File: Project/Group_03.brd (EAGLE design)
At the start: 100 x 80 mm, 29 parts, among them J1 POWER_JACKPTH_LOCK, U1 +12v, U3 TCA9546APW, U4 TMUX1208RSV

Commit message: Moved CY8CKIT
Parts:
- moved U$1 3.81 mm to (55.9, 34.3)
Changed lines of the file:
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@@
 <attribute name="VALUE" x="19.177" y="73.66" size="0.6096" layer="27" font="vector" ratio="20" rot="R270" align="top-center"/>
 </element>
-<element name="U$1" library="CY8KIT-059" package="CY8CKIT-059_TARGET" value="CY8CKIT-059_TARGET" x="55.88" y="38.1" smashed="yes" rot="R270"/>
+<element name="U$1" library="CY8KIT-059" package="CY8CKIT-059_TARGET" value="CY8CKIT-059_TARGET" x="55.88" y="34.29" smashed="yes" rot="R270"/>
 <element name="U1" library="SparkFun-IC-Power" package="TO-252" value="+12v" x="7.62" y="60.96" smashed="yes" rot="R90">
 <attribute name="NAME" x="10.16" y="57.15" size="1.27" layer="25" rot="R180"/>
@@
 <wire x1="76.87" y1="63.43" x2="82.423" y2="71.12" width="0" layer="19" extent="1-1"/>
 <wire x1="78.27" y1="62.43" x2="76.87" y2="63.43" width="0" layer="19" extent="1-1"/>
-<wire x1="64.77" y1="71.12" x2="76.87" y2="63.43" width="0" layer="19" extent="1-1"/>
+<wire x1="64.77" y1="67.31" x2="76.87" y2="63.43" width="0" layer="19" extent="1-1"/>
 <wire x1="77.735" y1="32.11" x2="78.27" y2="62.43" width="0" layer="19" extent="1-1"/>
-<wire x1="25.273" y1="62.23" x2="64.77" y2="71.12" width="0" layer="19" extent="1-1"/>
+<wire x1="25.273" y1="62.23" x2="64.77" y2="67.31" width="0" layer="19" extent="1-1"/>
 <wire x1="12.42" y1="63.24" x2="25.273" y2="62.23" width="0" layer="19" extent="1-1"/>
 <wire x1="3.81" y1="40.64" x2="12.42" y2="63.24" width="0" layer="19" extent="1-1"/>
 <wire x1="22.86" y1="37.37" x2="3.81" y2="40.64" width="0" layer="19" extent="1-1"/>
 <wire x1="22.86" y1="31.75" x2="22.86" y2="37.37" width="0" layer="19" extent="1-1"/>
-<wire x1="44.45" y1="7.62" x2="22.86" y2="31.75" width="0" layer="19" extent="1-1"/>
+<wire x1="44.45" y1="3.81" x2="22.86" y2="31.75" width="0" layer="19" extent="1-1"/>
 </signal>
 <signal name="GND">
@@
 <contactref element="U4" pad="12"/>
 <wire x1="78.27" y1="62.83" x2="85.217" y2="71.12" width="0" layer="19" extent="1-1"/>
-<wire x1="64.77" y1="68.58" x2="78.27" y2="62.83" width="0" layer="19" extent="1-1"/>
+<wire x1="64.77" y1="64.77" x2="78.27" y2="62.83" width="0" layer="19" extent="1-1"/>
 <wire x1="79.035" y1="26.31" x2="78.27" y2="62.83" width="0" layer="19" extent="1-1"/>
 <wire x1="82.285" y1="26.31" x2="79.035" y2="26.31" width="0" layer="19" extent="1-1"/>
-<wire x1="28.067" y1="62.23" x2="64.77" y2="68.58" width="0" layer="19" extent="1-1"/>
+<wire x1="28.067" y1="62.23" x2="64.77" y2="64.77" width="0" layer="19" extent="1-1"/>
 <wire x1="21.22" y1="64.77" x2="28.067" y2="62.23" width="0" layer="19" extent="1-1"/>
 <wire x1="25.4" y1="52.07" x2="28.067" y2="62.23" width="0" layer="19" extent="1-1"/>
@@
 <wire x1="22.86" y1="29.21" x2="22.86" y2="47.84" width="0" layer="19" extent="1-1"/>
 <wire x1="3.81" y1="38.1" x2="22.86" y2="29.21" width="0" layer="19" extent="1-1"/>
-<wire x1="44.45" y1="10.16" x2="22.86" y2="29.21" width="0" layer="19" extent="1-1"/>
+<wire x1="44.45" y1="6.35" x2="22.86" y2="29.21" width="0" layer="19" extent="1-1"/>
 </signal>
 <signal name="PHOTO_OUT">
@@
 <contactref element="R11" pad="2"/>
 <contactref element="U$1" pad="44"/>
-<wire x1="22.86" y1="46.14" x2="44.45" y2="50.8" width="0" layer="19" extent="1-1"/>
+<wire x1="22.86" y1="46.14" x2="44.45" y2="46.99" width="0" layer="19" extent="1-1"/>
 <wire x1="22.86" y1="41.37" x2="22.86" y2="46.14" width="0" layer="19" extent="1-1"/>
 </signal>
@@
 <contactref element="U2" pad="2"/>
 <contactref element="U$1" pad="43"/>
-<wire x1="24.765" y1="30.48" x2="44.45" y2="48.26" width="0" layer="19" extent="1-1"/>
+<wire x1="24.765" y1="30.48" x2="44.45" y2="44.45" width="0" layer="19" extent="1-1"/>
 </signal>
 <signal name="I2C_SCL_0">
@@
 <contactref element="U3" pad="1"/>
 <contactref element="U$1" pad="6"/>
-<wire x1="64.77" y1="20.32" x2="77.735" y2="26.31" width="0" layer="19" extent="1-1"/>
+<wire x1="64.77" y1="16.51" x2="77.735" y2="26.31" width="0" layer="19" extent="1-1"/>
 </signal>
 <signal name="I2C_A1">
 <contactref element="U3" pad="2"/>
 <contactref element="U$1" pad="7"/>
-<wire x1="64.77" y1="22.86" x2="78.385" y2="26.31" width="0" layer="19" extent="1-1"/>
+<wire x1="64.77" y1="19.05" x2="78.385" y2="26.31" width="0" layer="19" extent="1-1"/>
 </signal>
 <signal name="I2C_A2">
 <contactref element="U3" pad="13"/>
 <contactref element="U$1" pad="8"/>
-<wire x1="64.77" y1="25.4" x2="79.685" y2="32.11" width="0" layer="19" extent="1-1"/>
+<wire x1="64.77" y1="21.59" x2="79.685" y2="32.11" width="0" layer="19" extent="1-1"/>
 </signal>
 <signal name="I2C_SDA">
 <contactref element="U3" pad="15"/>
 <contactref element="U$1" pad="15"/>
-<wire x1="64.77" y1="43.18" x2="78.385" y2="32.11" width="0" layer="19" extent="1-1"/>
+<wire x1="64.77" y1="39.37" x2="78.385" y2="32.11" width="0" layer="19" extent="1-1"/>
 </signal>
 <signal name="I2C_SCL">
 <contactref element="U3" pad="14"/>
 <contactref element="U$1" pad="16"/>
-<wire x1="64.77" y1="45.72" x2="79.035" y2="32.11" width="0" layer="19" extent="1-1"/>
+<wire x1="64.77" y1="41.91" x2="79.035" y2="32.11" width="0" layer="19" extent="1-1"/>
 </signal>
 <signal name="N$3">
 <contactref element="U$1" pad="32"/>
 <contactref element="J6" pad="1"/>
-<wire x1="2.54" y1="6.35" x2="44.45" y2="20.32" width="0" layer="19" extent="1-1"/>
+<wire x1="2.54" y1="6.35" x2="44.45" y2="16.51" width="0" layer="19" extent="1-1"/>
 </signal>
 <signal name="N$4">
 <contactref element="U$1" pad="33"/>
 <contactref element="J6" pad="2"/>
-<wire x1="2.794" y1="8.89" x2="44.45" y2="22.86" width="0" layer="19" extent="1-1"/>
+<wire x1="2.794" y1="8.89" x2="44.45" y2="19.05" width="0" layer="19" extent="1-1"/>
 </signal>
 <signal name="N$5">
 <contactref element="U$1" pad="34"/>
 <contactref element="J6" pad="3"/>
-<wire x1="2.54" y1="11.43" x2="44.45" y2="25.4" width="0" layer="19" extent="1-1"/>
+<wire x1="2.54" y1="11.43" x2="44.45" y2="21.59" width="0" layer="19" extent="1-1"/>
 </signal>
 <signal name="N$6">
 <contactref element="U$1" pad="35"/>
 <contactref element="J6" pad="4"/>
-<wire x1="2.794" y1="13.97" x2="44.45" y2="27.94" width="0" layer="19" extent="1-1"/>
+<wire x1="2.794" y1="13.97" x2="44.45" y2="24.13" width="0" layer="19" extent="1-1"/>
 </signal>
 <signal name="N$7">
 <contactref element="U$1" pad="36"/>
 <contactref element="J6" pad="5"/>
-<wire x1="2.54" y1="16.51" x2="44.45" y2="30.48" width="0" layer="19" extent="1-1"/>
+<wire x1="2.54" y1="16.51" x2="44.45" y2="26.67" width="0" layer="19" extent="1-1"/>
 </signal>
 <signal name="N$8">
 <contactref element="U$1" pad="37"/>
 <contactref element="J6" pad="6"/>
-<wire x1="2.794" y1="19.05" x2="44.45" y2="33.02" width="0" layer="19" extent="1-1"/>
+<wire x1="2.794" y1="19.05" x2="44.45" y2="29.21" width="0" layer="19" extent="1-1"/>
 </signal>
 <signal name="N$9">
 <contactref element="U$1" pad="51"/>
 <contactref element="D1" pad="A"/>
-<wire x1="39.6" y1="55.88" x2="44.45" y2="68.58" width="0" layer="19" extent="1-1"/>
+<wire x1="39.6" y1="55.88" x2="44.45" y2="64.77" width="0" layer="19" extent="1-1"/>
 </signal>
 <signal name="N$11">
@@
 <contactref element="U$1" pad="21"/>
 <contactref element="U4" pad="6"/>
-<wire x1="64.77" y1="58.42" x2="77.27" y2="61.03" width="0" layer="19" extent="1-1"/>
+<wire x1="64.77" y1="54.61" x2="77.27" y2="61.03" width="0" layer="19" extent="1-1"/>
 </signal>
 <signal name="MUX_A2">
 <contactref element="U$1" pad="22"/>
 <contactref element="U4" pad="13"/>
-<wire x1="64.77" y1="60.96" x2="78.07" y2="63.43" width="0" layer="19" extent="1-1"/>
+<wire x1="64.77" y1="57.15" x2="78.07" y2="63.43" width="0" layer="19" extent="1-1"/>
 </signal>
 <signal name="MUX_A1">
 <contactref element="U$1" pad="23"/>
 <contactref element="U4" pad="14"/>
-<wire x1="64.77" y1="63.5" x2="77.67" y2="63.43" width="0" layer="19" extent="1-1"/>
+<wire x1="64.77" y1="59.69" x2="77.67" y2="63.43" width="0" layer="19" extent="1-1"/>
 </signal>
 <signal name="MUX_A0">
 <contactref element="U$1" pad="24"/>
 <contactref element="U4" pad="15"/>
-<wire x1="64.77" y1="66.04" x2="77.27" y2="63.43" width="0" layer="19" extent="1-1"/>
+<wire x1="64.77" y1="62.23" x2="77.27" y2="63.43" width="0" layer="19" extent="1-1"/>
 </signal>
 <signal name="N$2">

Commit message: First board layout attempt
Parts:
- moved J6 99.6 mm to (97.8, 35.6)
- moved J7 35.2 mm to (19.1, 6.35)
- moved R5 24.4 mm to (92.7, 17.8), turned to 270 degrees
- moved R4 23.4 mm to (92.7, 21.6), turned to 90 degrees
- moved R3 21.6 mm to (92.7, 2.54), turned to 90 degrees
- moved R11 19.0 mm to (41.9, 47.0)
- moved U2 16.6 mm to (39.4, 31.8)
- moved R2 16.5 mm to (92.7, 6.35), turned to 90 degrees
- moved U4 15.2 mm to (92.7, 62.2)
- moved R7 14.5 mm to (92.7, 25.4), turned to 90 degrees
- moved R10 14.0 mm to (36.8, 39.4)
- moved U3 13.7 mm to (85.1, 16.5)
- moved R1 13.3 mm to (41.9, 55.9), turned to 90 degrees
- moved J4 12.7 mm to (97.8, 22.9), turned to 90 degrees
- moved J2 12.7 mm to (97.8, 10.2), turned to 90 degrees
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
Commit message: Parts placement (size 73.66x71.12)
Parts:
- moved J7 37.0 mm to (55.9, 10.2), turned to 270 degrees
- moved D1 36.8 mm to (15.2, 39.4)
- moved R1 36.8 mm to (15.2, 30.5)
- moved R11 36.8 mm to (15.2, 21.6)
- moved R10 34.3 mm to (10.2, 17.8)
- moved S1 27.5 mm to (5.08, 58.4)
- moved R2 27.1 mm to (66.0, 11.4)
- moved R3 27.1 mm to (66.0, 7.62)
- moved R4 27.1 mm to (66.0, 26.7)
- moved R5 27.1 mm to (66.0, 22.9)
- moved R6 27.1 mm to (66.0, 34.3)
- moved R7 27.1 mm to (66.0, 30.5)
- moved R8 27.1 mm to (66.0, 19.1)
- moved R9 27.1 mm to (66.0, 15.2)
- moved J2 26.8 mm to (71.1, 7.62)
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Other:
- board size 100 x 80 mm -> 73.7 x 71.1 mm

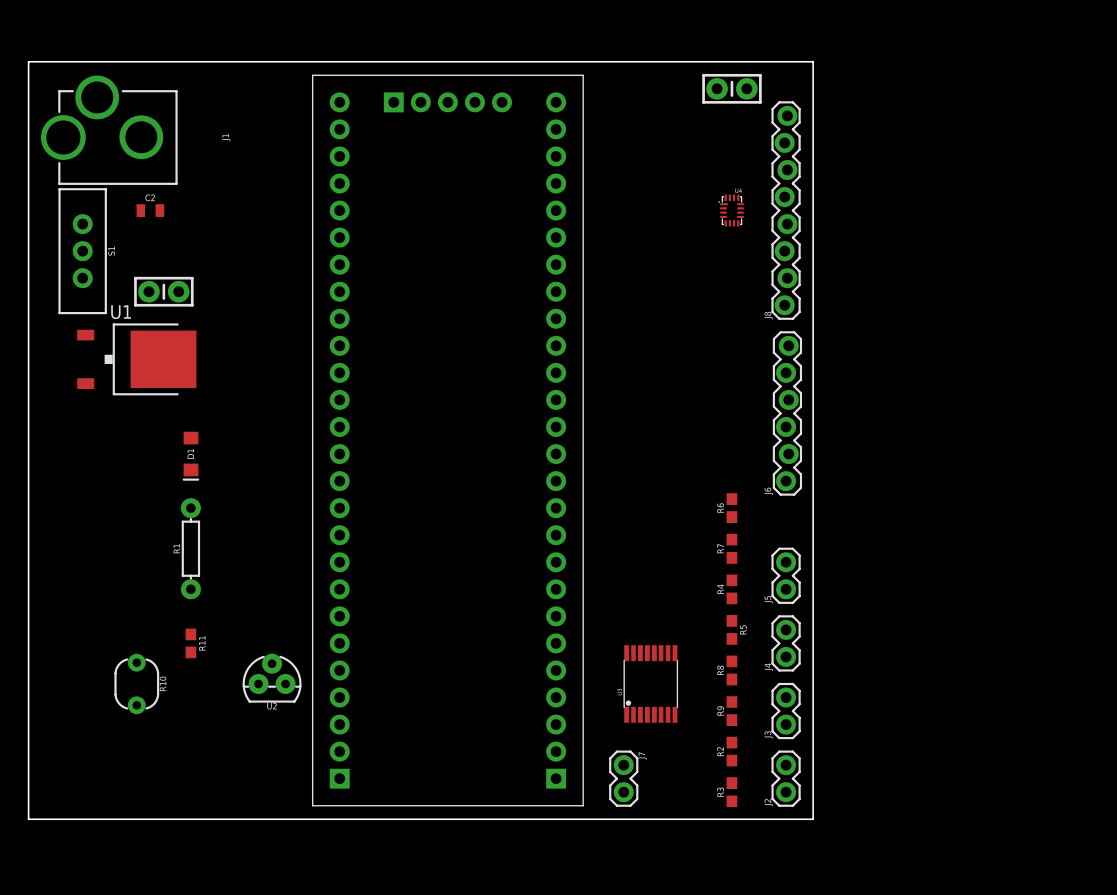
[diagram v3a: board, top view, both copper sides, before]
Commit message: Blue vias version (71.12x60.96)
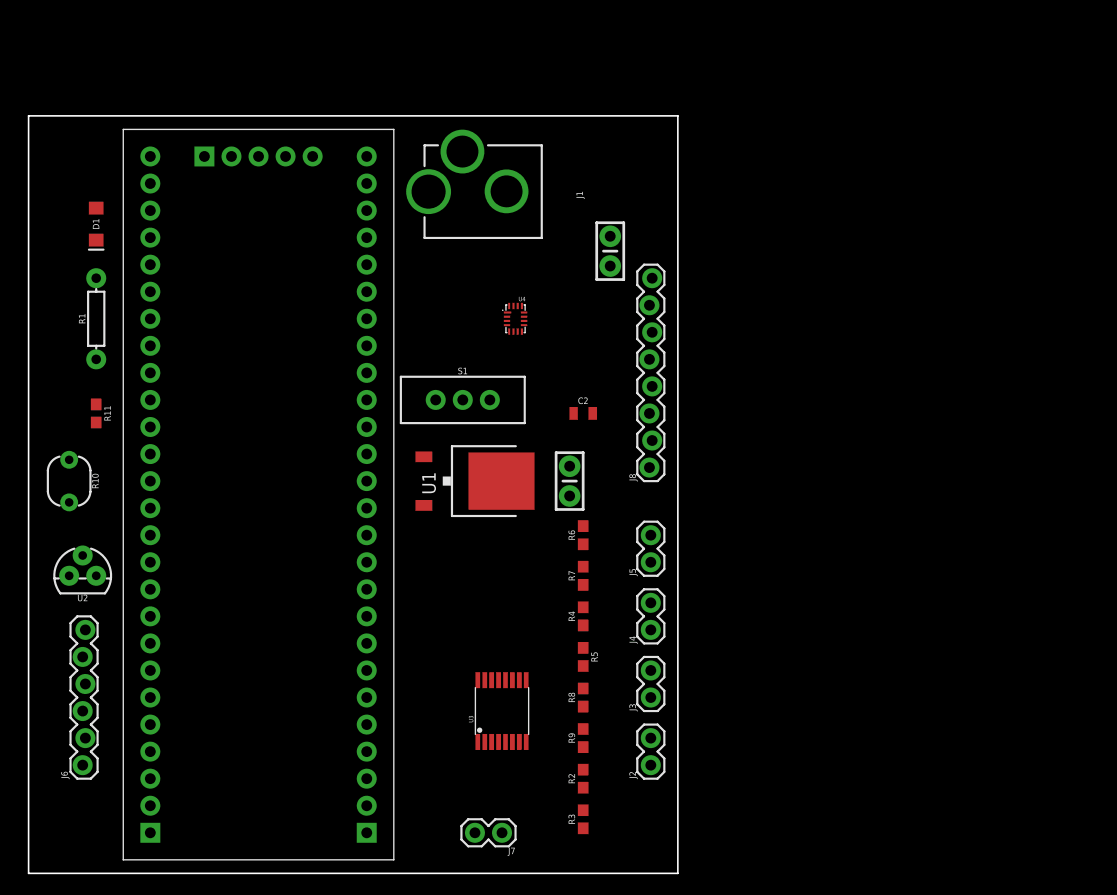
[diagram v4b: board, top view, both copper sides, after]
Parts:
- moved J6 71.2 mm to (5.08, 10.2)
- moved C2 44.9 mm to (52.1, 43.2)
- moved C3 42.0 mm to (50.8, 36.8), turned to 90 degrees
- moved S1 38.3 mm to (40.8, 44.5), turned to 270 degrees
- moved J1 34.7 mm to (51.4, 64.0)
- moved U1 33.7 mm to (41.9, 36.8)
- moved D1 23.3 mm to (6.35, 61.0)
- moved R1 23.3 mm to (6.35, 52.1)
- moved R11 23.3 mm to (6.35, 43.2)
- moved U4 22.7 mm to (45.7, 52.1)
- moved U2 20.5 mm to (5.08, 27.9)
- moved R10 20.1 mm to (3.81, 36.8)
- moved J8 19.8 mm to (58.4, 38.1)
- moved C1 19.1 mm to (54.6, 58.4), turned to 90 degrees
- moved U$1 18.5 mm to (22.9, 34.3)
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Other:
- board size 73.7 x 71.1 mm -> 61 x 71.1 mm

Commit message: Completed wiring, and design rules update
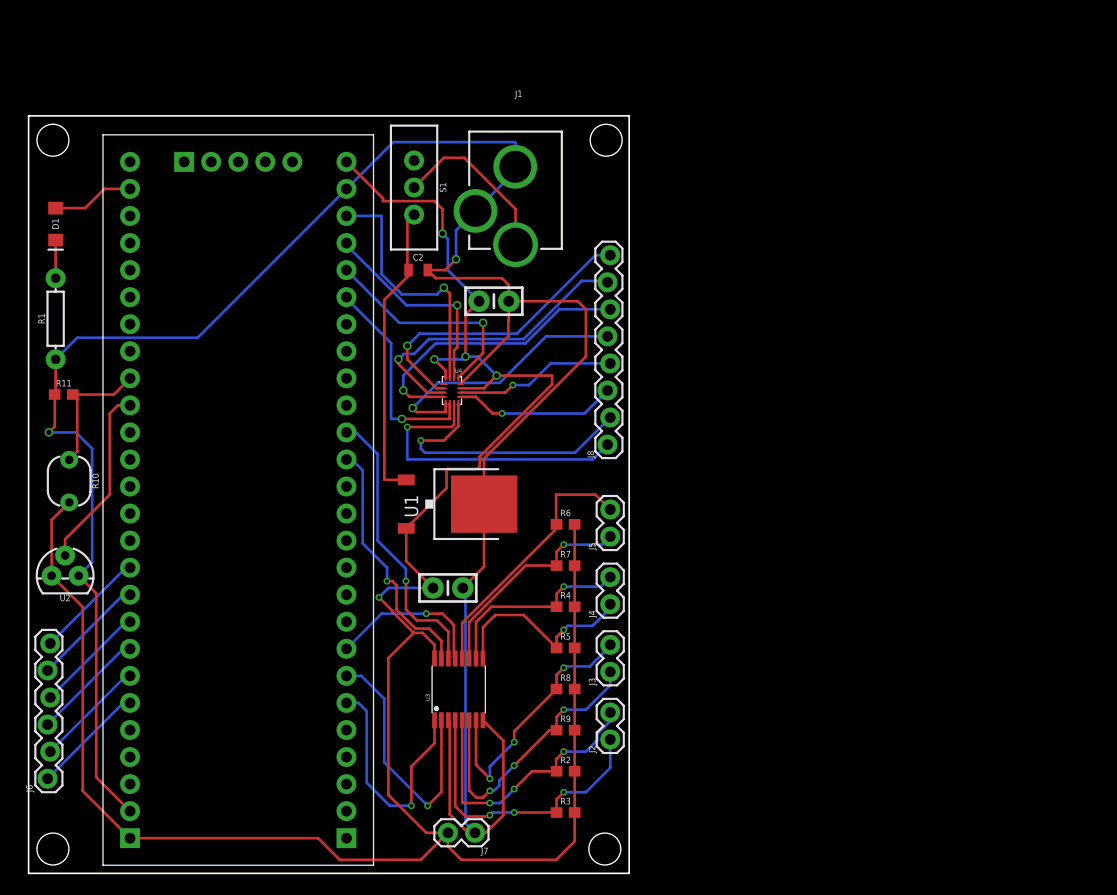
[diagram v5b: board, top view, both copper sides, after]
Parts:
- moved C2 20.5 mm to (36.6, 56.6)
- moved S1 20.5 mm to (36.2, 64.4), turned to 180 degrees
- moved C3 15.2 mm to (39.4, 26.8), turned to 0 degrees
- moved C1 11.9 mm to (43.7, 53.7), turned to 0 degrees
- moved J1 10.6 mm to (45.7, 72.9), turned to 180 degrees
- moved U4 9.00 mm to (39.8, 45.3)
- moved U3 4.54 mm to (40.4, 17.3)
- moved J2 4.51 mm to (54.6, 12.6)
- moved J4 4.51 mm to (54.6, 25.3)
- moved J5 4.51 mm to (54.6, 31.6)
- moved J3 4.51 mm to (54.6, 18.9)
- moved J8 4.49 mm to (54.5, 40.3)
- moved D1 3.81 mm to (2.54, 61.0)
- moved R1 3.81 mm to (2.54, 52.1)
- moved J6 3.54 mm to (1.78, 8.89)
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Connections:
- removed net N$10: R2.2, R3.2, R4.2, R5.2, R6.2, R7.2, R8.2, R9.2
- net 5V: now also R2.2, R3.2, R4.2, R5.2, R6.2, R7.2, R8.2, R9.2
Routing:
- net GND: track 0.00 -> 222.7 mm, vias 0 -> 2
- net 5V: track 0.00 -> 221.3 mm, vias 0 -> 5
- net N$18: track 0.00 -> 28.9 mm, vias 0 -> 1
- net N$12: track 0.00 -> 28.5 mm, vias 0 -> 1
- net N$2: track 0.00 -> 28.4 mm, vias 0 -> 1
- net I2C_SDA_0: track 0.00 -> 28.3 mm, vias 0 -> 3
- net 12V: track 0.00 -> 28.2 mm
- net N$13: track 0.00 -> 27.4 mm, vias 0 -> 1
- net I2C_SCL: track 0.00 -> 26.8 mm, vias 0 -> 1
- net I2C_SDA_1: track 0.00 -> 26.8 mm, vias 0 -> 3
- net I2C_SCL_0: track 0.00 -> 26.7 mm, vias 0 -> 3
- net N$17: track 0.00 -> 26.3 mm, vias 0 -> 1
- net N$14: track 0.00 -> 25.1 mm, vias 0 -> 1
- net I2C_SCL_3: track 0.00 -> 24.7 mm
- net I2C_A1: track 0.00 -> 24.7 mm, vias 0 -> 1
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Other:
- board size 61 x 71.1 mm -> 56.4 x 71.1 mm

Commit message: Silkscreen names
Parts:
- moved R2 1.27 mm to (49.1, 9.58)
- moved R3 1.27 mm to (49.1, 5.71)
- moved R4 1.27 mm to (49.1, 25.0)
- moved R5 1.27 mm to (49.1, 21.2)
- moved R6 1.27 mm to (49.1, 32.8)
- moved R7 1.27 mm to (49.1, 28.9)
- moved R8 1.27 mm to (49.1, 17.3)
- moved R9 1.27 mm to (49.1, 13.4)
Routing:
- net N$9: track 7.73 -> 10.9 mm
- net I2C_SCL_3: track 24.7 -> 25.5 mm
- net I2C_SDA_0: track 28.3 -> 27.6 mm
- net I2C_SCL_1: track 24.6 -> 25.4 mm
- net 5V: track 221.3 -> 220.8 mm
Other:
- board text added: "10K"
- board text added: "BLUE LED"
- board text added: "C1"
- board text added: "C2"
- board text added: "C3"
- board text added: "CY8CKIT"
- board text added: "J2"
- board text added: "J3"
- board text added: "J4"
- board text added: "J5"
- board text added: "J6"
- board text added: "J7"
- board text added: "J8"
- board text added: "PHOTOCELL"
- board text added: "POWER JACK"
- board text added: "R1"
- board text added: "R11"
- board text added: "R2"
- board text added: "R3"
- board text added: "R4"
- board text added: "R5"
- board text added: "R6"
- board text added: "R7"
- board text added: "R8"
- board text added: "R9"
- board text added: "S1"
- board text added: "TCA9546A"
- board text added: "TEMP"
- board text added: "TMUX1208"

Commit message: Copper pour both layers
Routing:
- net N$9: track 10.9 -> 7.73 mm
- net I2C_SCL_1: track 25.4 -> 23.1 mm
- net I2C_SDA_1: track 26.8 -> 25.5 mm
- added copper zone on layer 16, net 5V
- added copper zone on layer 1, net GND
